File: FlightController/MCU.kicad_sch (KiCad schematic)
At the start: 24 parts, among them U3 STM32F411CEUx, Y1 25MHz_GND24

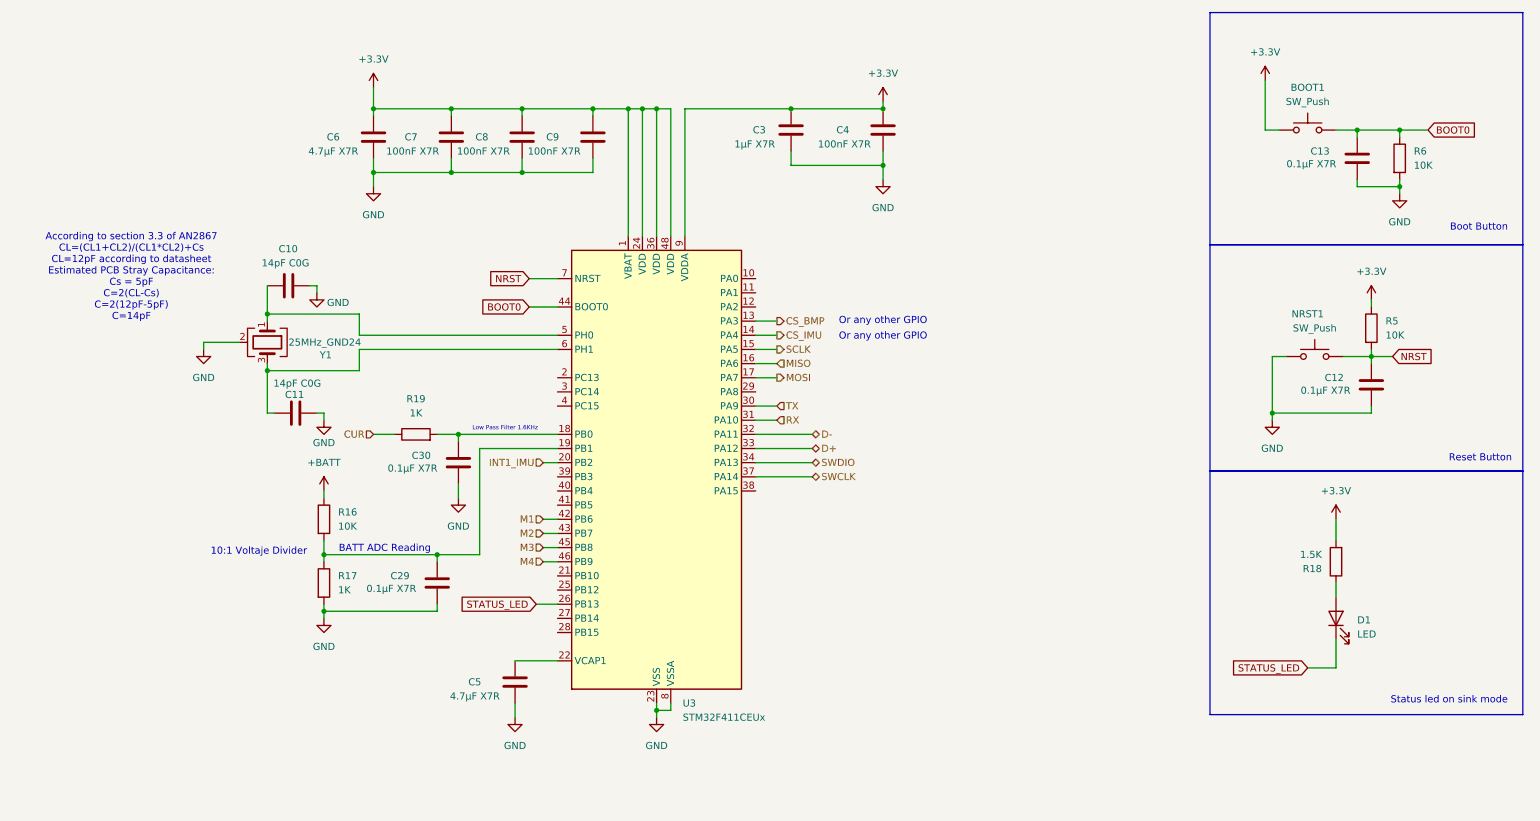
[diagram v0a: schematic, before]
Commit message: Added Part numbers and Buck in PCB
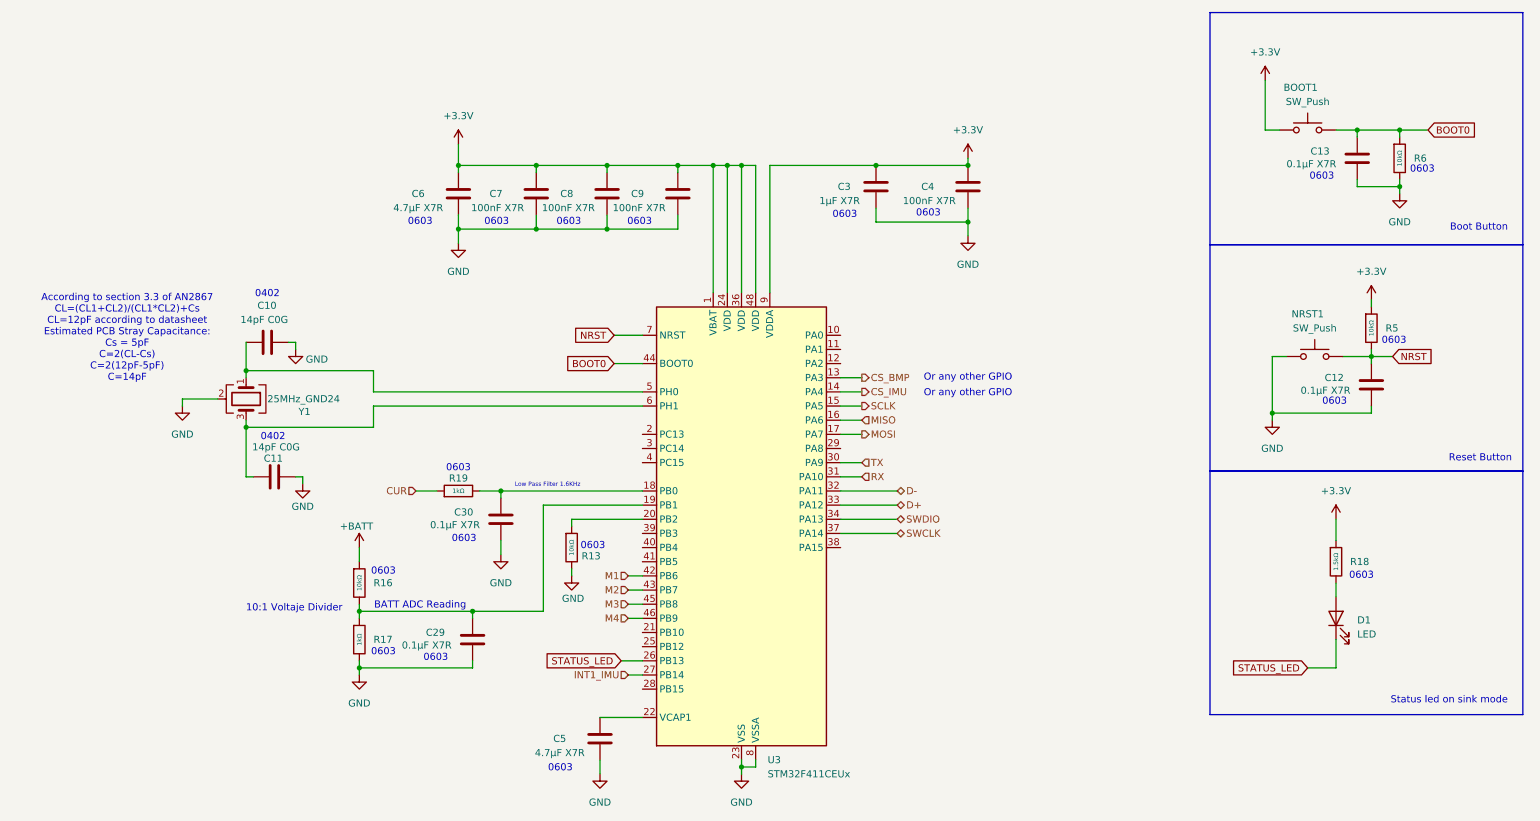
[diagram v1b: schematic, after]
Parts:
- removed R16, R5, R6: 10K, Resistor_SMD:R_1206_3216Metric_Pad1.30x1.75mm_HandSolder, symbol Device:R
- removed R17, R19: 1K, Resistor_SMD:R_1206_3216Metric_Pad1.30x1.75mm_HandSolder, symbol Device:R
- removed R18: 1.5K, Resistor_SMD:R_1206_3216Metric_Pad1.30x1.75mm_HandSolder, symbol Device:R
- added R13, R16, R5, R6: 10kΩ, PCM_JLCPCB:R_0603, symbol PCM_JLCPCB-Resistors:0603,10kΩ
- added R17, R19: 1kΩ, PCM_JLCPCB:R_0603, symbol PCM_JLCPCB-Resistors:0603,1kΩ
- added R18: 1.5kΩ, PCM_JLCPCB:R_0603, symbol PCM_JLCPCB-Resistors:0603,1.5kΩ
- BOOT1, NRST1: footprint Button_Switch_SMD:SW_SPST_PTS810 -> PCM_JLCPCB:SW_TS-1088-AR02016; LCSC (none) -> C720477
- C10, C11: LCSC (none) -> C5360816
- C12, C13, C29, C30: footprint Capacitor_SMD:C_1206_3216Metric_Pad1.33x1.80mm_HandSolder -> Capacitor_SMD:C_0603_1608Metric_Pad1.08x0.95mm_HandSolder; LCSC (none) -> C1590
- C3: footprint Capacitor_SMD:C_1206_3216Metric_Pad1.33x1.80mm_HandSolder -> Capacitor_SMD:C_0603_1608Metric_Pad1.08x0.95mm_HandSolder; LCSC (none) -> C5199872
- C4, C7, C8, C9: footprint Capacitor_SMD:C_1206_3216Metric_Pad1.33x1.80mm_HandSolder -> Capacitor_SMD:C_0603_1608Metric_Pad1.08x0.95mm_HandSolder; LCSC (none) -> C49326605
- C5, C6: footprint Capacitor_SMD:C_1206_3216Metric_Pad1.33x1.80mm_HandSolder -> Capacitor_SMD:C_0603_1608Metric_Pad1.08x0.95mm_HandSolder; LCSC (none) -> C6119822
- D1: LCSC (none) -> C2286
- U3: now left out of the parts list
- Y1: LCSC (none) -> C9006
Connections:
- net +3.3V: now also R18.1, R5.1
- net +BATT: now also R16.1
- net BOOT0: now also R6.1
- net CUR: now also R19.1
- net GND: now also R13.2, R17.2, R6.2
- net INT1_IMU: now also U3.27 (PB14); no longer U3.20 (PB2)
- net NRST: now also R5.2
- net at C29.1, U3.19 (PB1): now also R16.2, R17.1
- net at D1.2 (A): now also R18.2
- net at C30.1, U3.18 (PB0): now also R19.2
- new net: R13.1, U3.20 (PB2)
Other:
- note added: "0402"
- note added: "0603"
- moved on the sheet: C10, C11, C29, C3, C30, C4, C5, C6, C7, C8, C9, U3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

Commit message: Update PCB
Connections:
- net M1: now also U3.46 (PB9); no longer U3.42 (PB6)
- net M2: now also U3.45 (PB8); no longer U3.43 (PB7)
- net M3: now also U3.43 (PB7); no longer U3.45 (PB8)
- net M4: now also U3.42 (PB6); no longer U3.46 (PB9)

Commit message: Final Update
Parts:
- removed BOOT1, NRST1: SW_Push, PCM_JLCPCB:SW_TS-1088-AR02016, symbol Switch:SW_Push
- added JP1: SolderJumper_2_Open, Jumper:SolderJumper-2_P1.3mm_Open_Pad1.0x1.5mm, symbol Jumper:SolderJumper_2_Open
- C4, C7, C8, C9: value 100nF X7R -> 0.1μF X7R; LCSC C49326605 -> C1590
- Y1: footprint Crystal:Crystal_SMD_3225-4Pin_3.2x2.5mm_HandSoldering -> CRYSTAL-SMD_4P-L3.2-W2.5-BL:CRYSTAL-SMD_4P-L3.2-W2.5-BL
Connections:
- net +3.3V: now also JP1.2 (B)
- net BOOT0: now also JP1.1 (A)
- net STATUS_LED: now also U3.41 (PB5); no longer U3.26 (PB13)
- net NRST: no longer names the net of C12.1, R5.2, U3.7 (NRST)
- no-connect marks 0 -> 14
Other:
- note added: "BOOT0"
- note removed: "Boot Button"
- note removed: "Or any other GPIO"
- note removed: "Reset Button"
- moved on the sheet: C12, C30, C6, D1, R13, R19, R5, R6
